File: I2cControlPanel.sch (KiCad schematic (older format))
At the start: 44 parts, among them J1 JoystickL, J2 Conn_01x06, J3 Conn_01x04, J4 Conn_01x04, J5 JoystickR, J6 Conn_01x04, SW6 SW_Push, U1 NJM12888F33, U2 ATmega328PB-MU, U3 AQM0802

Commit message: Assign 0402 condensor for 0.1uf
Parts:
- C1, C4, C5, C6: footprint Capacitor_SMD:C_0603_1608Metric -> Capacitor_SMD:C_0402_1005Metric
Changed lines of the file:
@@
 F 0 "C4" V 5352 2600 50  0000 C CNN
 F 1 "0.1u" V 5261 2600 50  0000 C CNN
-F 2 "Capacitor_SMD:C_0603_1608Metric" H 5138 2450 50  0001 C CNN
+F 2 "Capacitor_SMD:C_0402_1005Metric" H 5138 2450 50  0001 C CNN
 F 3 "~" H 5100 2600 50  0001 C CNN
 	1    5100 2600
@@
 F 0 "C1" H 2665 1446 50  0000 L CNN
 F 1 "0.1u" H 2665 1355 50  0000 L CNN
-F 2 "Capacitor_SMD:C_0603_1608Metric" H 2588 1250 50  0001 C CNN
+F 2 "Capacitor_SMD:C_0402_1005Metric" H 2588 1250 50  0001 C CNN
 F 3 "~" H 2550 1400 50  0001 C CNN
 	1    2550 1400
@@
 F 0 "C5" H 7515 5304 50  0000 L CNN
 F 1 "0.1u" H 7515 5395 50  0000 L CNN
-F 2 "Capacitor_SMD:C_0603_1608Metric" H 7438 5200 50  0001 C CNN
+F 2 "Capacitor_SMD:C_0402_1005Metric" H 7438 5200 50  0001 C CNN
 F 3 "~" H 7400 5350 50  0001 C CNN
 	1    7400 5350
@@
 F 0 "C6" H 7515 5704 50  0000 L CNN
 F 1 "0.1u" H 7515 5795 50  0000 L CNN
-F 2 "Capacitor_SMD:C_0603_1608Metric" H 7438 5600 50  0001 C CNN
+F 2 "Capacitor_SMD:C_0402_1005Metric" H 7438 5600 50  0001 C CNN
 F 3 "~" H 7400 5750 50  0001 C CNN
 	1    7400 5750

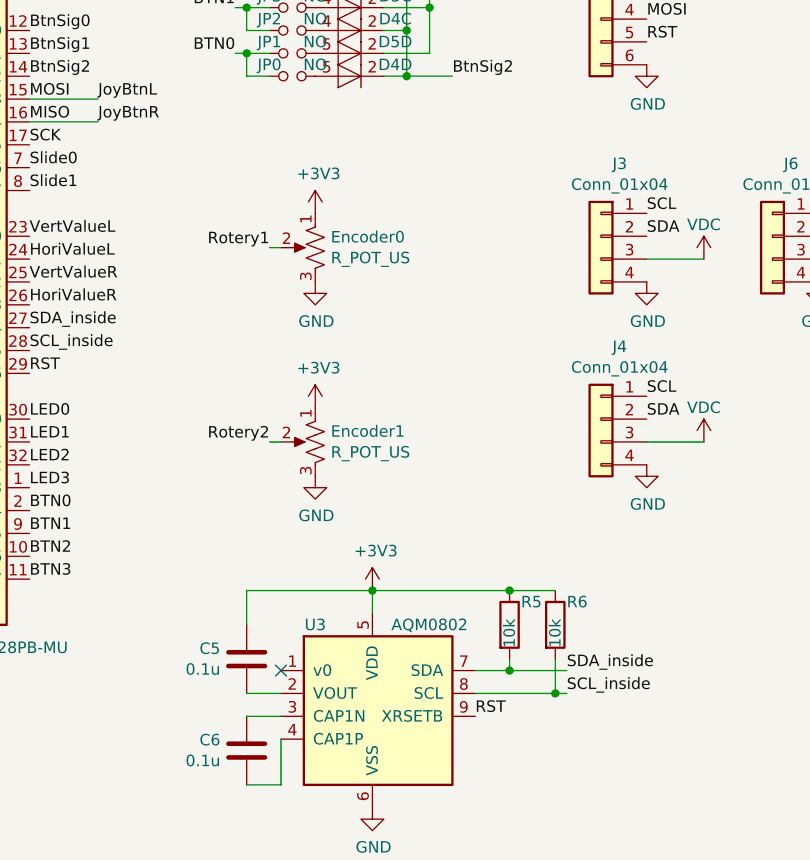
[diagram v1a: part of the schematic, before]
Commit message: Change rotery encoder and remove pull up for internal i2c
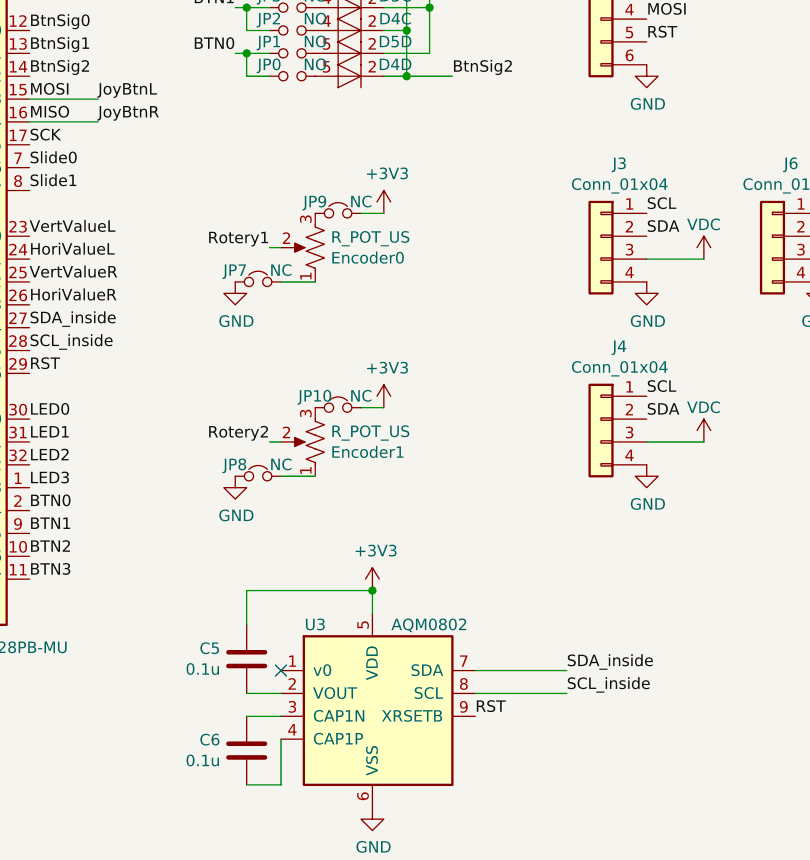
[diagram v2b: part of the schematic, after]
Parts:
- removed R5, R6: 10k, Resistor_SMD:R_0603_1608Metric, symbol Device:R
- added JP10, JP7, JP8, JP9: NC, Jumper:SolderJumper-2_P1.3mm_Bridged_RoundedPad1.0x1.5mm, symbol I2cControlPanel-rescue:Jumper_NC_Small-Device
- Encoder0, Encoder1: footprint my-kicad-footprints:Volume -> my-kicad-footprints:RoteryEncoderWithPowerLabel
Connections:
- net +3V3: now also JP10.2, JP9.2; no longer Encoder0.1, Encoder1.1
- net GND: now also JP7.1, JP8.1; no longer Encoder0.3, Encoder1.3
- new net: Encoder0.1, JP7.2
- new net: Encoder0.3, JP9.1
- new net: Encoder1.1, JP8.2
- new net: Encoder1.3, JP10.1
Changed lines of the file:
@@
 VertValueR
 Wire Wire Line
-	8550 5050 8750 5050
-Connection ~ 8550 5050
-Wire Wire Line
-	8750 5500 8800 5500
-Connection ~ 8750 5500
-Wire Wire Line
-	8750 5350 8750 5500
-Wire Wire Line
-	8550 5400 8800 5400
-Connection ~ 8550 5400
-Wire Wire Line
-	8550 5350 8550 5400
-Wire Wire Line
-	8400 5400 8550 5400
-Wire Wire Line
-	8400 5500 8750 5500
-Wire Wire Line
 	7950 5050 7950 5150
 Wire Wire Line
 	7400 5050 7400 5200
-$Comp
-L Device:R R6
-U 1 1 5EE5E7B0
-P 8750 5200
-F 0 "R6" H 8800 5300 50  0000 L CNN
-F 1 "10k" V 8750 5100 50  0000 L CNN
-F 2 "Resistor_SMD:R_0603_1608Metric" V 8680 5200 50  0001 C CNN
-F 3 "~" H 8750 5200 50  0001 C CNN
-	1    8750 5200
-	1    0    0    -1
-$EndComp
-$Comp
-L Device:R R5
-U 1 1 5EE5BCBA
-P 8550 5200
-F 0 "R5" H 8600 5300 50  0000 L CNN
-F 1 "10k" V 8550 5100 50  0000 L CNN
-F 2 "Resistor_SMD:R_0603_1608Metric" V 8480 5200 50  0001 C CNN
-F 3 "~" H 8550 5200 50  0001 C CNN
-	1    8550 5200
-	1    0    0    -1
-$EndComp
 Text Label 8800 5500 0    50   ~ 0
 SCL_inside
@@
 F 0 "Encoder0" H 7632 3596 50  0000 R CNN
 F 1 "R_POT_US" H 7632 3505 50  0000 R CNN
-F 2 "my-kicad-footprints:Volume" H 7700 3550 50  0001 C CNN
+F 2 "my-kicad-footprints:RoteryEncoderWithPowerLabel" H 7700 3550 50  0001 C CNN
 F 3 "~" H 7700 3550 50  0001 C CNN
 	1    7700 3550
-	-1   0    0    -1
-$EndComp
-$Comp
-L power:+3V3 #PWR0123
-U 1 1 5EE80F27
-P 7700 3400
-F 0 "#PWR0123" H 7700 3250 50  0001 C CNN
-F 1 "+3V3" H 7715 3573 50  0000 C CNN
-F 2 "" H 7700 3400 50  0001 C CNN
-F 3 "" H 7700 3400 50  0001 C CNN
-	1    7700 3400
-	1    0    0    -1
-$EndComp
-$Comp
-L power:GND #PWR0124
-U 1 1 5EE8236B
-P 7700 3700
-F 0 "#PWR0124" H 7700 3450 50  0001 C CNN
-F 1 "GND" H 7705 3527 50  0000 C CNN
-F 2 "" H 7700 3700 50  0001 C CNN
-F 3 "" H 7700 3700 50  0001 C CNN
-	1    7700 3700
-	1    0    0    -1
+	-1   0    0    1
 $EndComp
 Text Label 7500 3550 2    50   ~ 0
@@
 F 0 "Encoder1" H 7632 4446 50  0000 R CNN
 F 1 "R_POT_US" H 7632 4355 50  0000 R CNN
-F 2 "my-kicad-footprints:Volume" H 7700 4400 50  0001 C CNN
+F 2 "my-kicad-footprints:RoteryEncoderWithPowerLabel" H 7700 4400 50  0001 C CNN
 F 3 "~" H 7700 4400 50  0001 C CNN
 	1    7700 4400
-	-1   0    0    -1
+	-1   0    0    1
 $EndComp
 $Comp
 L power:+3V3 #PWR0130
 U 1 1 5EE88746
-P 7700 4250
-F 0 "#PWR0130" H 7700 4100 50  0001 C CNN
-F 1 "+3V3" H 7715 4423 50  0000 C CNN
-F 2 "" H 7700 4250 50  0001 C CNN
-F 3 "" H 7700 4250 50  0001 C CNN
-	1    7700 4250
+P 8000 4250
+F 0 "#PWR0130" H 8000 4100 50  0001 C CNN
+F 1 "+3V3" H 8015 4423 50  0000 C CNN
+F 2 "" H 8000 4250 50  0001 C CNN
+F 3 "" H 8000 4250 50  0001 C CNN
+	1    8000 4250
 	1    0    0    -1
 $EndComp
@@
 L power:GND #PWR0131
 U 1 1 5EE8874C
-P 7700 4550
-F 0 "#PWR0131" H 7700 4300 50  0001 C CNN
-F 1 "GND" H 7705 4377 50  0000 C CNN
-F 2 "" H 7700 4550 50  0001 C CNN
-F 3 "" H 7700 4550 50  0001 C CNN
-	1    7700 4550
+P 7350 4550
+F 0 "#PWR0131" H 7350 4300 50  0001 C CNN
+F 1 "GND" H 7355 4377 50  0000 C CNN
+F 2 "" H 7350 4550 50  0001 C CNN
+F 3 "" H 7350 4550 50  0001 C CNN
+	1    7350 4550
 	1    0    0    -1
 $EndComp
@@
 RST
 Wire Wire Line
-	7950 5050 8550 5050
-Wire Wire Line
 	2550 1000 2550 1100
 Wire Wire Line
@@
 Wire Wire Line
 	4150 3850 4150 4250
+$Comp
+L I2cControlPanel-rescue:Jumper_NC_Small-Device JP10
+U 1 1 608FA385
+P 7800 4250
+F 0 "JP10" H 7700 4300 50  0000 C CNN
+F 1 "NC" H 7900 4300 50  0000 C CNN
+F 2 "Jumper:SolderJumper-2_P1.3mm_Bridged_RoundedPad1.0x1.5mm" H 7800 4250 50  0001 C CNN
+F 3 "~" H 7800 4250 50  0001 C CNN
+	1    7800 4250
+	1    0    0    -1
+$EndComp
+$Comp
+L power:GND #PWR0124
+U 1 1 5EE8236B
+P 7350 3700
+F 0 "#PWR0124" H 7350 3450 50  0001 C CNN
+F 1 "GND" H 7355 3527 50  0000 C CNN
+F 2 "" H 7350 3700 50  0001 C CNN
+F 3 "" H 7350 3700 50  0001 C CNN
+	1    7350 3700
+	1    0    0    -1
+$EndComp
+$Comp
+L power:+3V3 #PWR0123
+U 1 1 5EE80F27
+P 8000 3400
+F 0 "#PWR0123" H 8000 3250 50  0001 C CNN
+F 1 "+3V3" H 8015 3573 50  0000 C CNN
+F 2 "" H 8000 3400 50  0001 C CNN
+F 3 "" H 8000 3400 50  0001 C CNN
+	1    8000 3400
+	1    0    0    -1
+$EndComp
+Wire Wire Line
+	8000 3400 7900 3400
+$Comp
+L I2cControlPanel-rescue:Jumper_NC_Small-Device JP7
+U 1 1 6090B9D4
+P 7450 3700
+F 0 "JP7" H 7350 3750 50  0000 C CNN
+F 1 "NC" H 7550 3750 50  0000 C CNN
+F 2 "Jumper:SolderJumper-2_P1.3mm_Bridged_RoundedPad1.0x1.5mm" H 7450 3700 50  0001 C CNN
+F 3 "~" H 7450 3700 50  0001 C CNN
+	1    7450 3700
+	1    0    0    -1
+$EndComp
+Wire Wire Line
+	7550 3700 7700 3700
+Wire Wire Line
+	8000 4250 7900 4250
+$Comp
+L I2cControlPanel-rescue:Jumper_NC_Small-Device JP9
+U 1 1 60926E98
+P 7800 3400
+F 0 "JP9" H 7700 3450 50  0000 C CNN
+F 1 "NC" H 7900 3450 50  0000 C CNN
+F 2 "Jumper:SolderJumper-2_P1.3mm_Bridged_RoundedPad1.0x1.5mm" H 7800 3400 50  0001 C CNN
+F 3 "~" H 7800 3400 50  0001 C CNN
+	1    7800 3400
+	1    0    0    -1
+$EndComp
+$Comp
+L I2cControlPanel-rescue:Jumper_NC_Small-Device JP8
+U 1 1 60927344
+P 7450 4550
+F 0 "JP8" H 7350 4600 50  0000 C CNN
+F 1 "NC" H 7550 4600 50  0000 C CNN
+F 2 "Jumper:SolderJumper-2_P1.3mm_Bridged_RoundedPad1.0x1.5mm" H 7450 4550 50  0001 C CNN
+F 3 "~" H 7450 4550 50  0001 C CNN
+	1    7450 4550
+	1    0    0    -1
+$EndComp
+Wire Wire Line
+	7550 4550 7700 4550
+Wire Wire Line
+	8400 5400 8800 5400
+Wire Wire Line
+	8400 5500 8800 5500
 $EndSCHEMATC
